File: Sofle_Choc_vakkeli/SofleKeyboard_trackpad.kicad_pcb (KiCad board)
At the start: 2 copper layers, 162.7 x 111.8 mm, 124 parts, among them J1 PimorioniTrackball, J2 4PIN, J3 OLED, P1 i2c_pin, P2 i2c_pin, SW1 SW_PUSH_LED, SW10 SW_PUSH_LED, SW11 SW_PUSH_LED, SW12 SW_PUSH_LED, SW13 SW_PUSH_LED, SW14 SW_PUSH_LED, SW15 SW_PUSH_LED, SW16 SW_PUSH_LED, SW17 SW_PUSH_LED, SW18 SW_PUSH_LED, SW19 SW_PUSH_LED, SW2 SW_PUSH_LED, SW20 SW_PUSH_LED, SW21 SW_PUSH_LED, SW22 SW_PUSH_LED, SW23 SW_PUSH_LED, SW24 SW_PUSH_LED, SW25 Rotary_Encoder_Switch, SW26 SW_PUSH_LED, SW27 SW_PUSH_LED, SW28 SW_PUSH_LED, SW29 SW_PUSH_LED, SW3 Rotary_Encoder_Switch, SW3 SW_PUSH_LED, SW30 SW_PUSH_LED, SW31 SW_PUSH_LED, SW32 SW_PUSH_LED, SW33 SW_PUSH_LED, SW34 SW_PUSH_LED, SW35 SW_PUSH_LED, SW4 SW_PUSH_LED, SW5 SW_PUSH_LED, SW6 SW_PUSH_LED, SW7 SW_PUSH_LED, SW8 SW_PUSH_LED, SW9 SW_PUSH_LED, U1 ProMicro

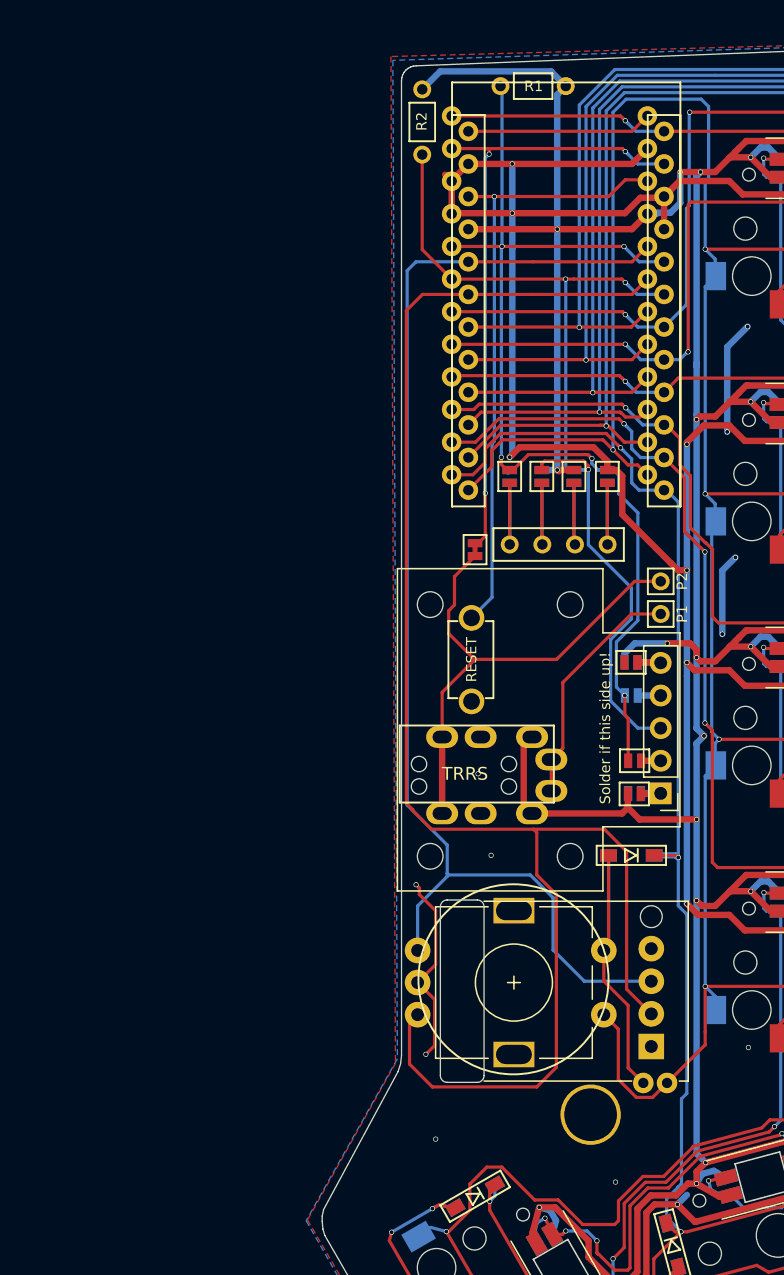
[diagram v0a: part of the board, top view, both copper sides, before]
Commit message: fixed single breakable button gnd, added dxf for 3d.
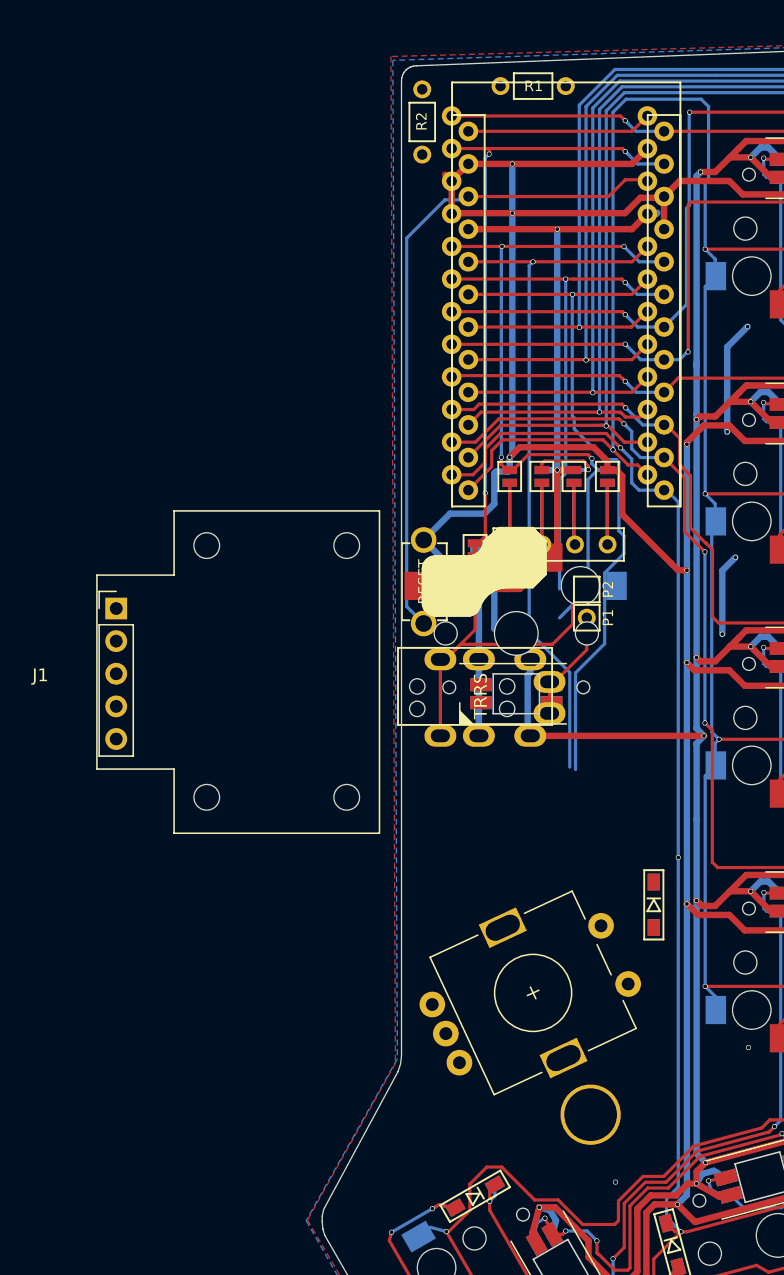
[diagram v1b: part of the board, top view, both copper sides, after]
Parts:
- removed JP10, JP15, JP16, JP9: Jumper_NO_Small, SofleKeyboard-footprint:Jumper
- removed JP12: Solder if this side up!, SofleKeyboard-footprint:Jumper
- removed JP13: Solder if this side up, SofleKeyboard-footprint:Jumper
- removed the SW3 at (101.6, 106.7)
- added SW32: SW_PUSH_LED, SofleChoc:Choc_Hotswap_SK6812MiniE, F.Cu at (97.2, 81.5)
- JP7: value Solder if this side up! -> Jumper_NO_Small
- moved J1 44.8 mm to (66.1, 79.6), turned to 0 degrees
- moved RSW1 7.12 mm to (90.0, 77.5), turned to 270 degrees
- moved J2 6.05 mm to (88.0, 85.7)
- moved P2 5.79 mm to (102.7, 78.1)
- moved P1 5.77 mm to (102.7, 80.3)
- moved D25 4.23 mm to (107.9, 102.7), turned to 270 degrees
- moved SW25 1.70 mm to (98.5, 109.5), turned to 25 degrees
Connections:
- J1 pad 3: SCL -> Net-(J1-Pad3)
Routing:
- net ENCB: track 126.5 -> 55.2 mm, vias 0 -> 1
- net ENCA: track 96.4 -> 55.2 mm, vias 0 -> 1
- net GND: track 1073.8 -> 1110.1 mm, vias 72 -> 67
- net SW25B: track 26.7 -> 0.00 mm
- net SCL: track 75.4 -> 49.6 mm
- net SDA: track 82.3 -> 57.5 mm, vias 5 -> 4
- net SW25A: track 214.4 -> 195.3 mm
- net VCC: track 1051.4 -> 1032.6 mm, vias 46 -> 43
- net /i2c_d: track 39.8 -> 29.6 mm
- net /i2c_c: track 18.7 -> 9.85 mm
- net row4: track 208.6 -> 204.1 mm
- net Net-(J1-Pad5): track 3.66 -> 0.00 mm
- net Net-(J1-Pad1): track 3.11 -> 0.00 mm
- net RESET: track 48.5 -> 51.2 mm, vias 1 -> 0
- net Net-(J1-Pad4): track 1.79 -> 0.00 mm
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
